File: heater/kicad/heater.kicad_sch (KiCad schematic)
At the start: 76 parts, among them J1 Conn_01x02_Pin, J2 Conn_01x02_Pin, J5 pcie_98, U1 OPA333, U10 B0509XT-1WR3, U14 OPA333, U15 LTC1968, U16 OPA333, U2 ESD5344D-TP, U4 TPS7A2050PDBVR, U5 ISO1541, U6 LTC1968, U7 OPA333, U8 ADS1115IDGS, U9 XC6206P332MR

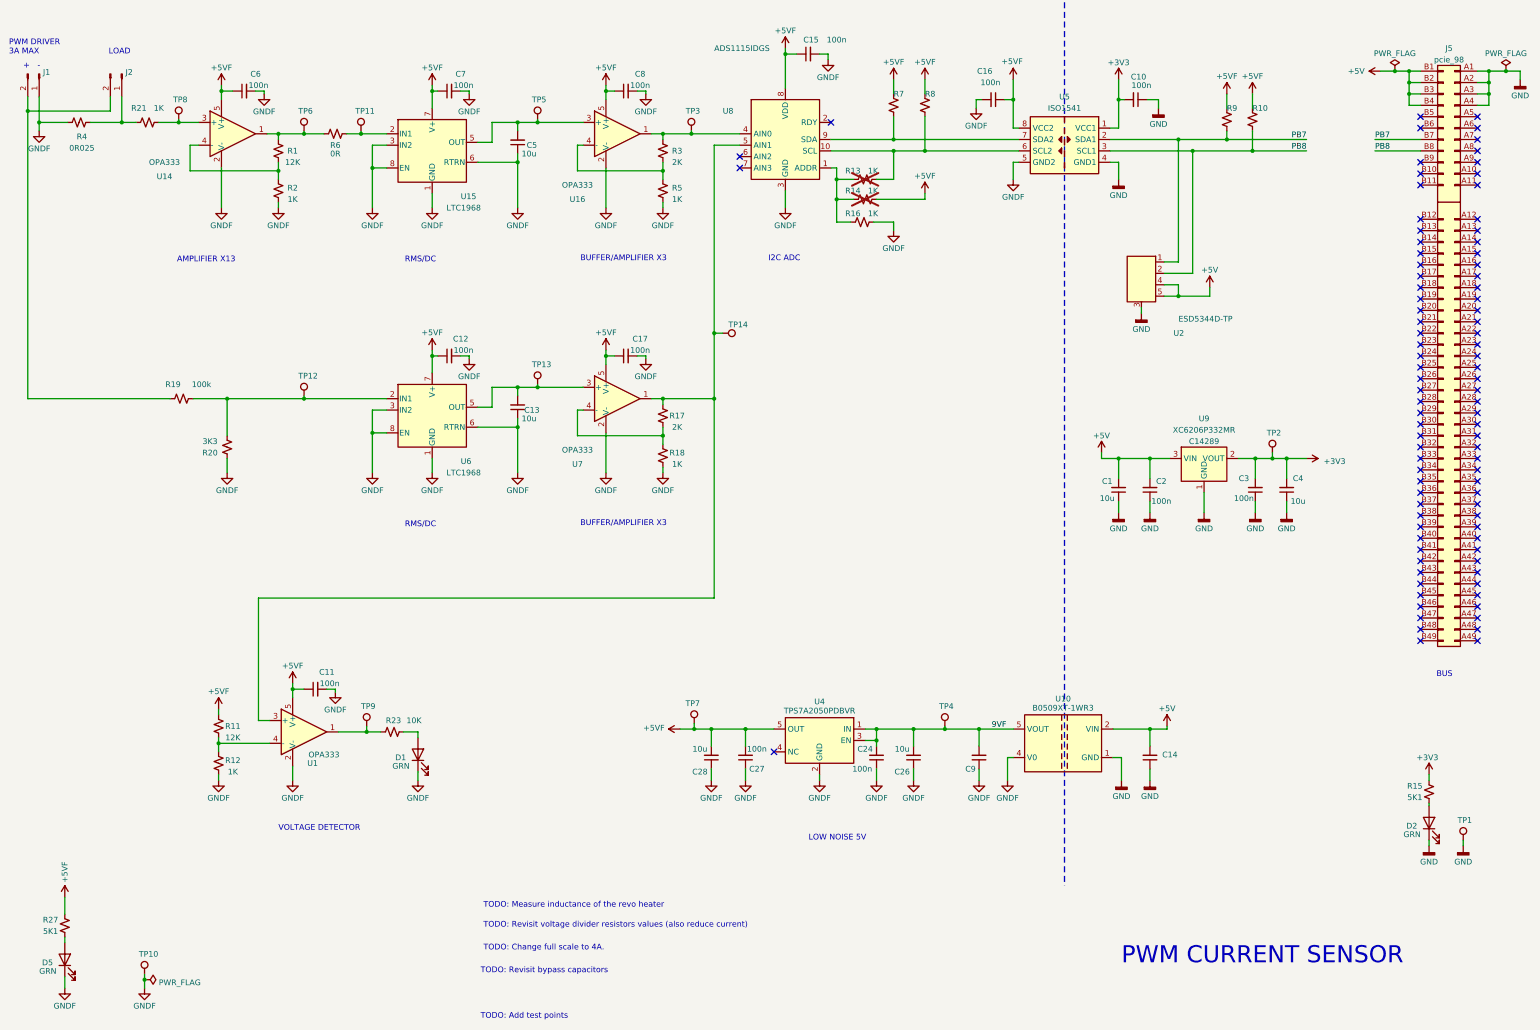
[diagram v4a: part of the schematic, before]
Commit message: Updated heater schematic
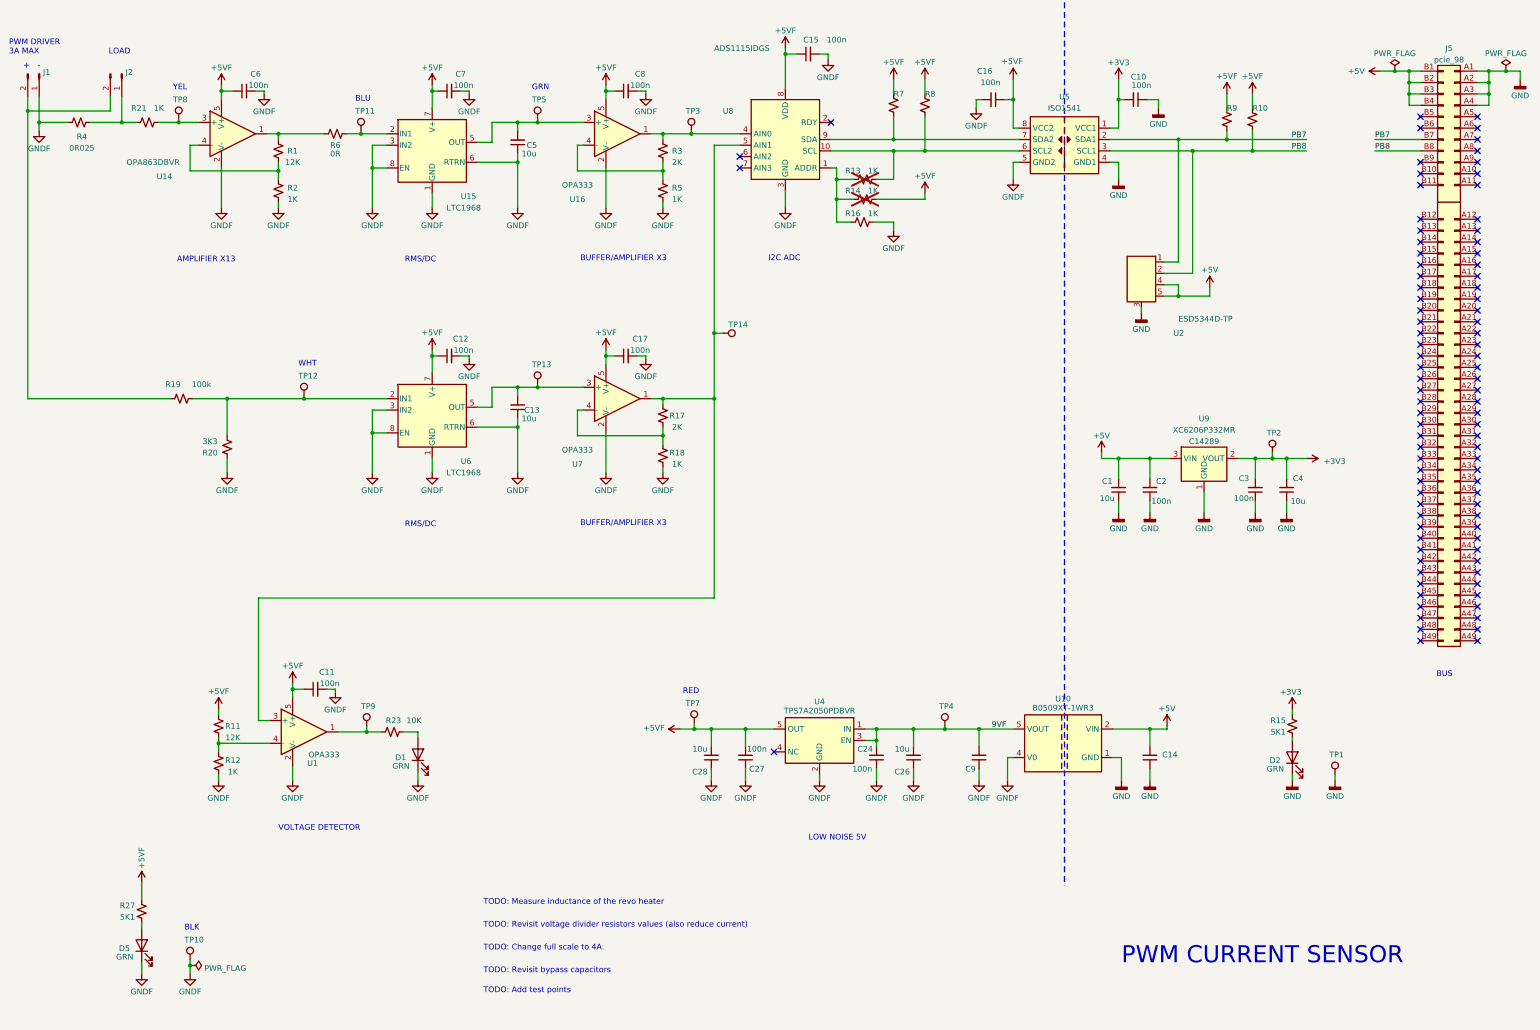
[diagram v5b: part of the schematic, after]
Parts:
- removed TP6: TestPoint, common:Test_Pad, symbol common:TestPoint
- U14: value OPA333 -> OPA863DBVR
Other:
- note added: "BLK"
- note added: "BLU"
- note added: "GRN"
- note added: "RED"
- note added: "WHT"
- note added: "YEL"
- moved on the sheet: D2, D5, R15, R27, TP1, TP10

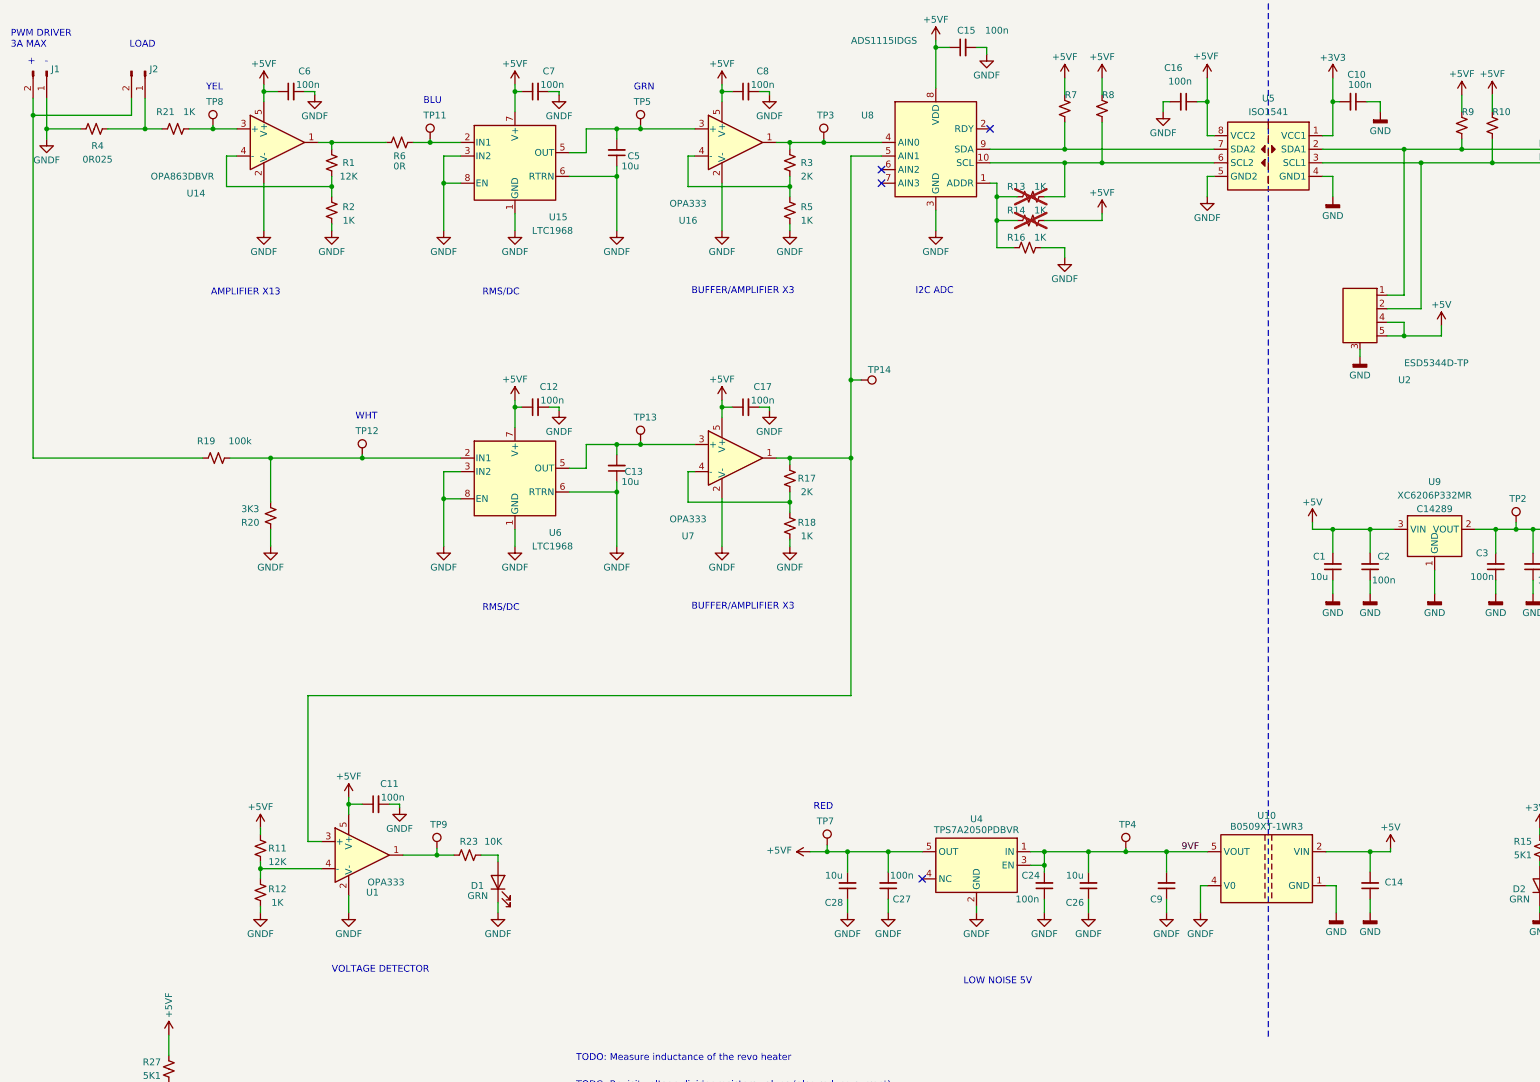
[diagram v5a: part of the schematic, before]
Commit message: Updated heater schematic.
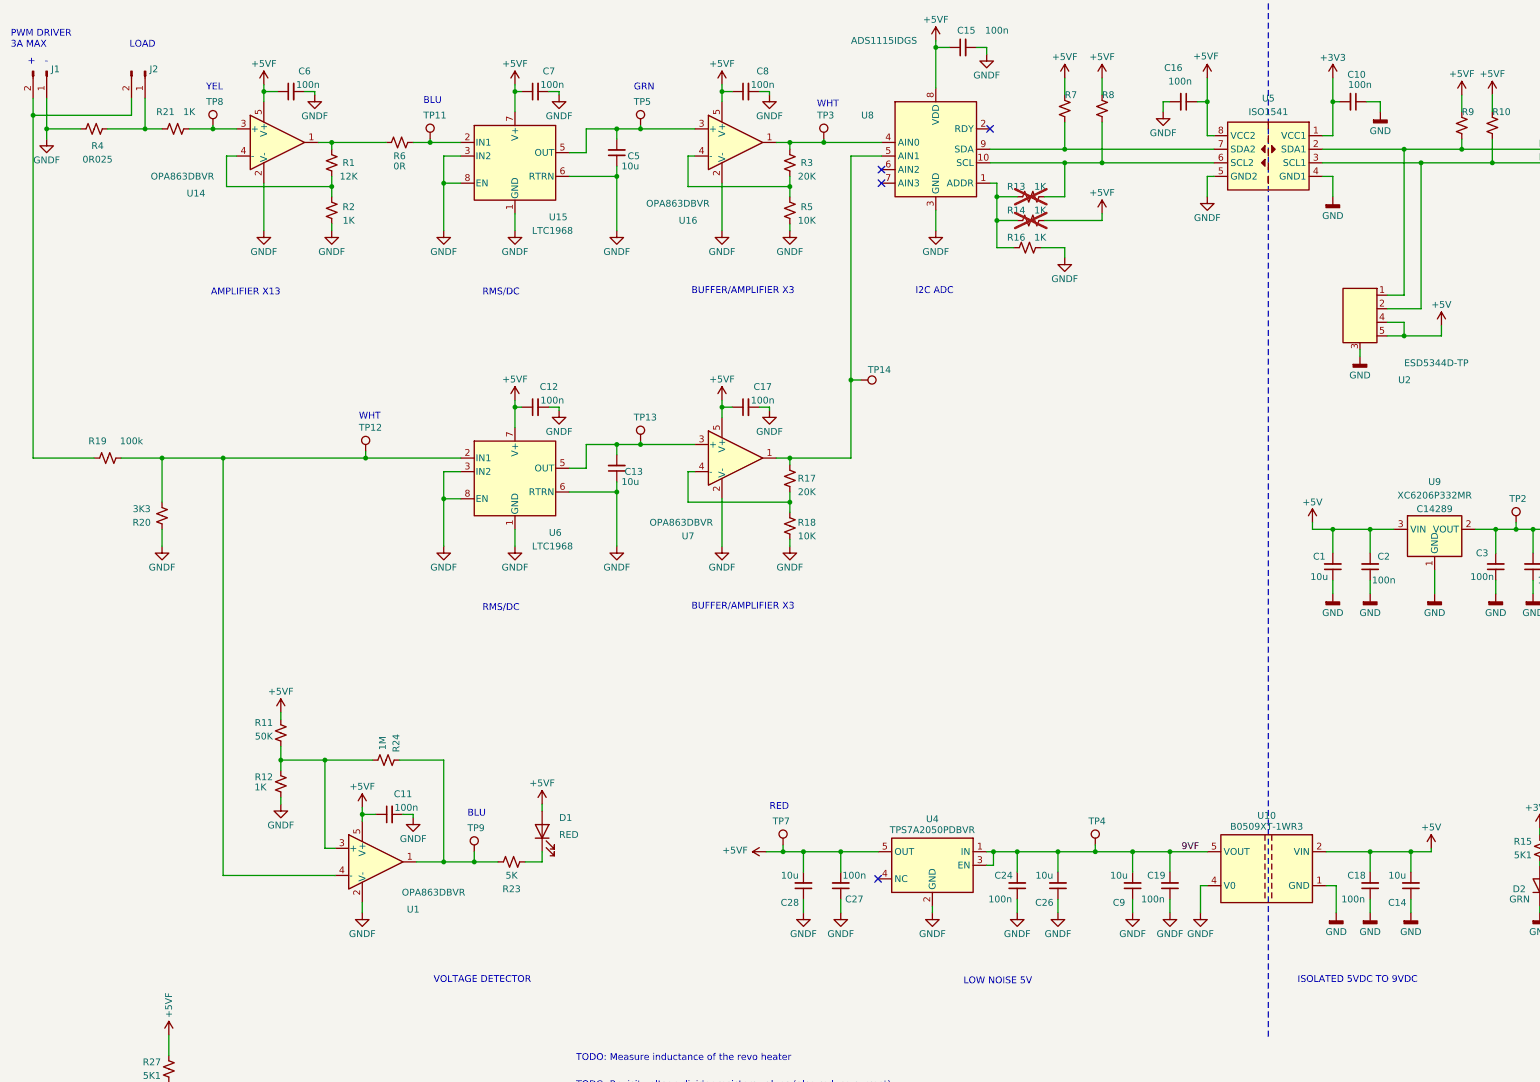
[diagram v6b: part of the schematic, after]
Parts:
- added C18, C19: 100n, Capacitor_SMD:C_0402_1005Metric, symbol Device:C_Small
- added R24: 1M, symbol Device:R_Small_US
- C14, C9: value ~ -> 10u; footprint (none) -> Capacitor_SMD:C_0603_1608Metric; LCSC (none) -> C19702
- D1: value GRN -> RED
- R11: value 12K -> 50K; LCSC C25752 -> (none)
- R17, R3: value 2K -> 20K; LCSC C4109 -> (none)
- R18: value 1K -> 10K
- R23: value 10K -> 5K; LCSC C25744 -> (none)
- R5: value 1K -> 10K; LCSC C11702 -> (none)
- U1, U16, U7: value OPA333 -> OPA863DBVR
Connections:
- net +5V: now also C18.2
- net +5VF: now also D1.2 (A)
- net 9VF: now also C19.2
- net GND: now also C18.1
- net GND1: now also C19.1; no longer D1.1 (K)
- net at R23.1, TP9.1, U1.1: now also R24.2
- net at R23.2: now also D1.1 (K); no longer D1.2 (A)
- net at R11.1, R12.2: now also U1.3 (+), R24.1; no longer U1.4 (-)
- net at R19.2, R20.1, TP12.1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: now also U1.4 (-)
- net at R17.2, TP14.1, U7.1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: no longer U1.3 (+)
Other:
- note added: "ISOLATED 5VDC TO 9VDC"
- moved on the sheet: C11, C24, C26, C27, C28, D1, R11, R12, R19, R20, R23, TP12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

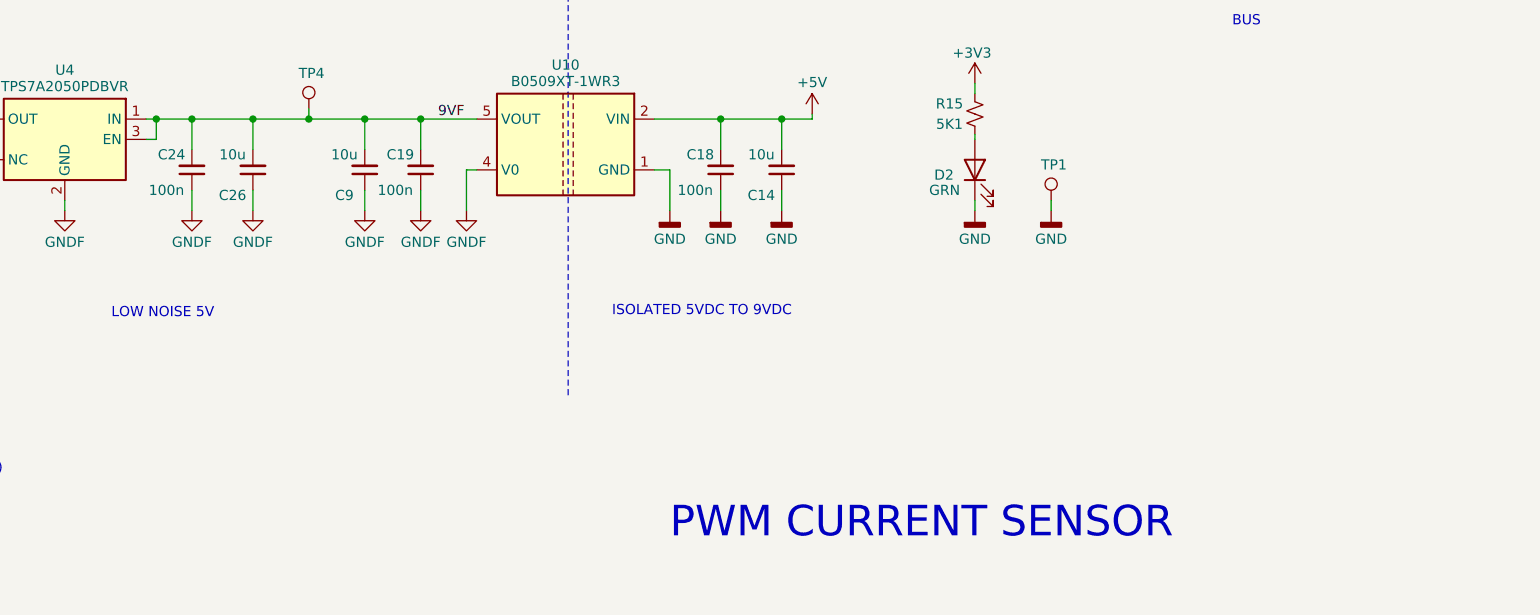
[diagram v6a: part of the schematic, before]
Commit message: Updated heater schematic.
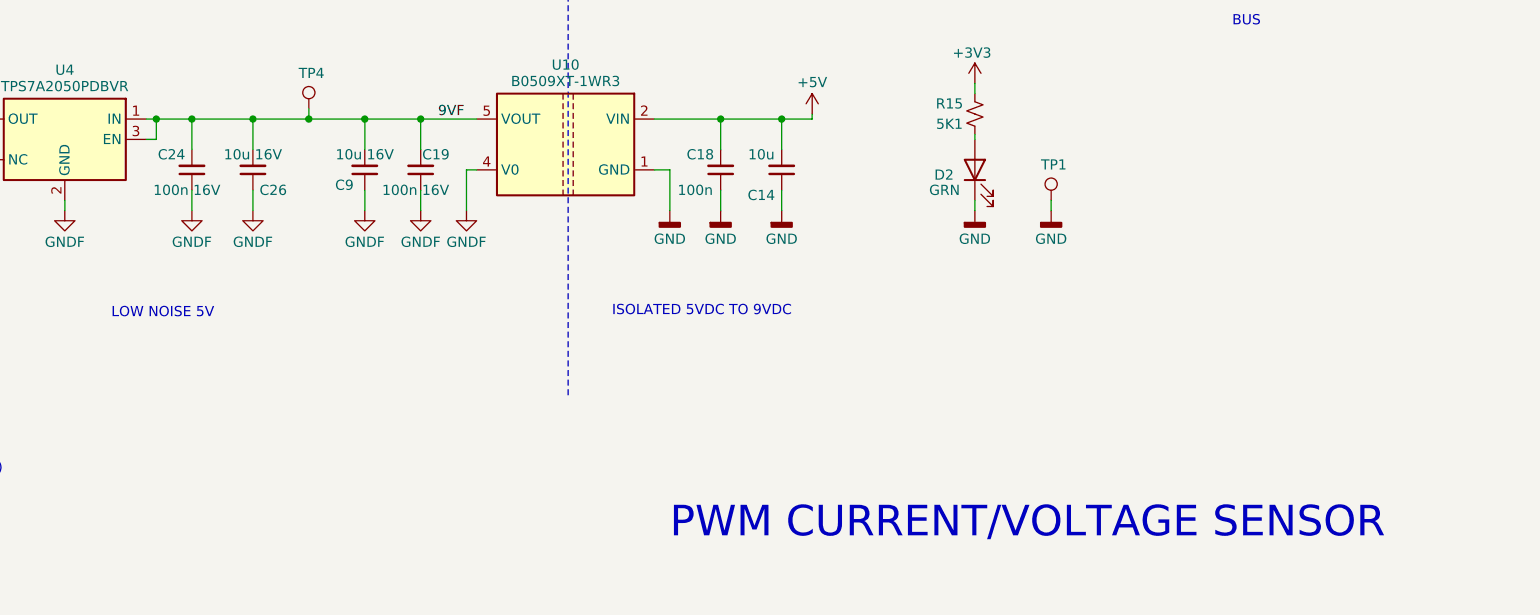
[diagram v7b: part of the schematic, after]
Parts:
- C19, C24: value 100n -> 100n 16V; footprint Capacitor_SMD:C_0402_1005Metric -> (none)
- C26, C9: value 10u -> 10u 16V; LCSC C19702 -> C96446
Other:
- note added: "PWM CURRENT/VOLTAGE SENSOR"
- note removed: "PWM CURRENT SENSOR"
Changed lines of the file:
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@@
     (effects (font (size 1.27 1.27)) (justify left bottom))
   )
-  (text "PWM CURRENT SENSOR" (at 267.97 246.38 0)
+  (text "PWM CURRENT/VOLTAGE SENSOR" (at 267.97 246.38 0)
     (effects (font (size 3.81 3.81)) (justify left bottom))
   )
@@
   (symbol (lib_id "Device:C_Small") (at 229.87 200.025 0) (mirror x) (unit 1)
     (in_bom yes) (on_board yes) (dnp no)
-    (property "Reference" "C9" (at 227.33 203.2 0)
+    (property "Reference" "C9" (at 227.33 201.93 0)
       (effects (font (size 1.27 1.27)))
     )
-    (property "Value" "10u" (at 227.33 198.12 0)
+    (property "Value" "10u 16V" (at 229.87 198.12 0)
       (effects (font (size 1.27 1.27)))
     )
@@
       (effects (font (size 1.27 1.27)) hide)
     )
-    (property "LCSC" "C19702" (at 229.87 200.025 0)
+    (property "LCSC" "C96446" (at 229.87 200.025 0)
       (effects (font (size 1.27 1.27)) hide)
     )
@@
       (effects (font (size 1.27 1.27)))
     )
-    (property "Value" "100n" (at 205.105 202.565 0)
+    (property "Value" "100n 16V" (at 207.645 202.565 0)
       (effects (font (size 1.27 1.27)))
     )
-    (property "Footprint" "Capacitor_SMD:C_0402_1005Metric" (at 208.28 200.025 0)
+    (property "Footprint" "" (at 208.28 200.025 0)
       (effects (font (size 1.27 1.27)) hide)
     )
@@
   (symbol (lib_id "Device:C_Small") (at 215.9 200.025 0) (mirror x) (unit 1)
     (in_bom yes) (on_board yes) (dnp no)
-    (property "Reference" "C26" (at 213.36 203.2 0)
+    (property "Reference" "C26" (at 218.44 202.565 0)
       (effects (font (size 1.27 1.27)))
     )
-    (property "Value" "10u" (at 213.36 198.12 0)
+    (property "Value" "10u 16V" (at 215.9 198.12 0)
       (effects (font (size 1.27 1.27)))
     )
@@
       (effects (font (size 1.27 1.27)) hide)
     )
-    (property "LCSC" "C19702" (at 215.9 200.025 0)
+    (property "LCSC" "C96446" (at 215.9 200.025 0)
       (effects (font (size 1.27 1.27)) hide)
     )
@@
   (symbol (lib_id "Device:C_Small") (at 236.855 200.025 180) (unit 1)
     (in_bom yes) (on_board yes) (dnp no)
-    (property "Reference" "C19" (at 234.315 198.12 0)
+    (property "Reference" "C19" (at 238.76 198.12 0)
       (effects (font (size 1.27 1.27)))
     )
-    (property "Value" "100n" (at 233.68 202.565 0)
+    (property "Value" "100n 16V" (at 236.22 202.565 0)
       (effects (font (size 1.27 1.27)))
     )
-    (property "Footprint" "Capacitor_SMD:C_0402_1005Metric" (at 236.855 200.025 0)
+    (property "Footprint" "" (at 236.855 200.025 0)
       (effects (font (size 1.27 1.27)) hide)
     )
